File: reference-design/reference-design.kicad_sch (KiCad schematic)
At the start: 21 parts

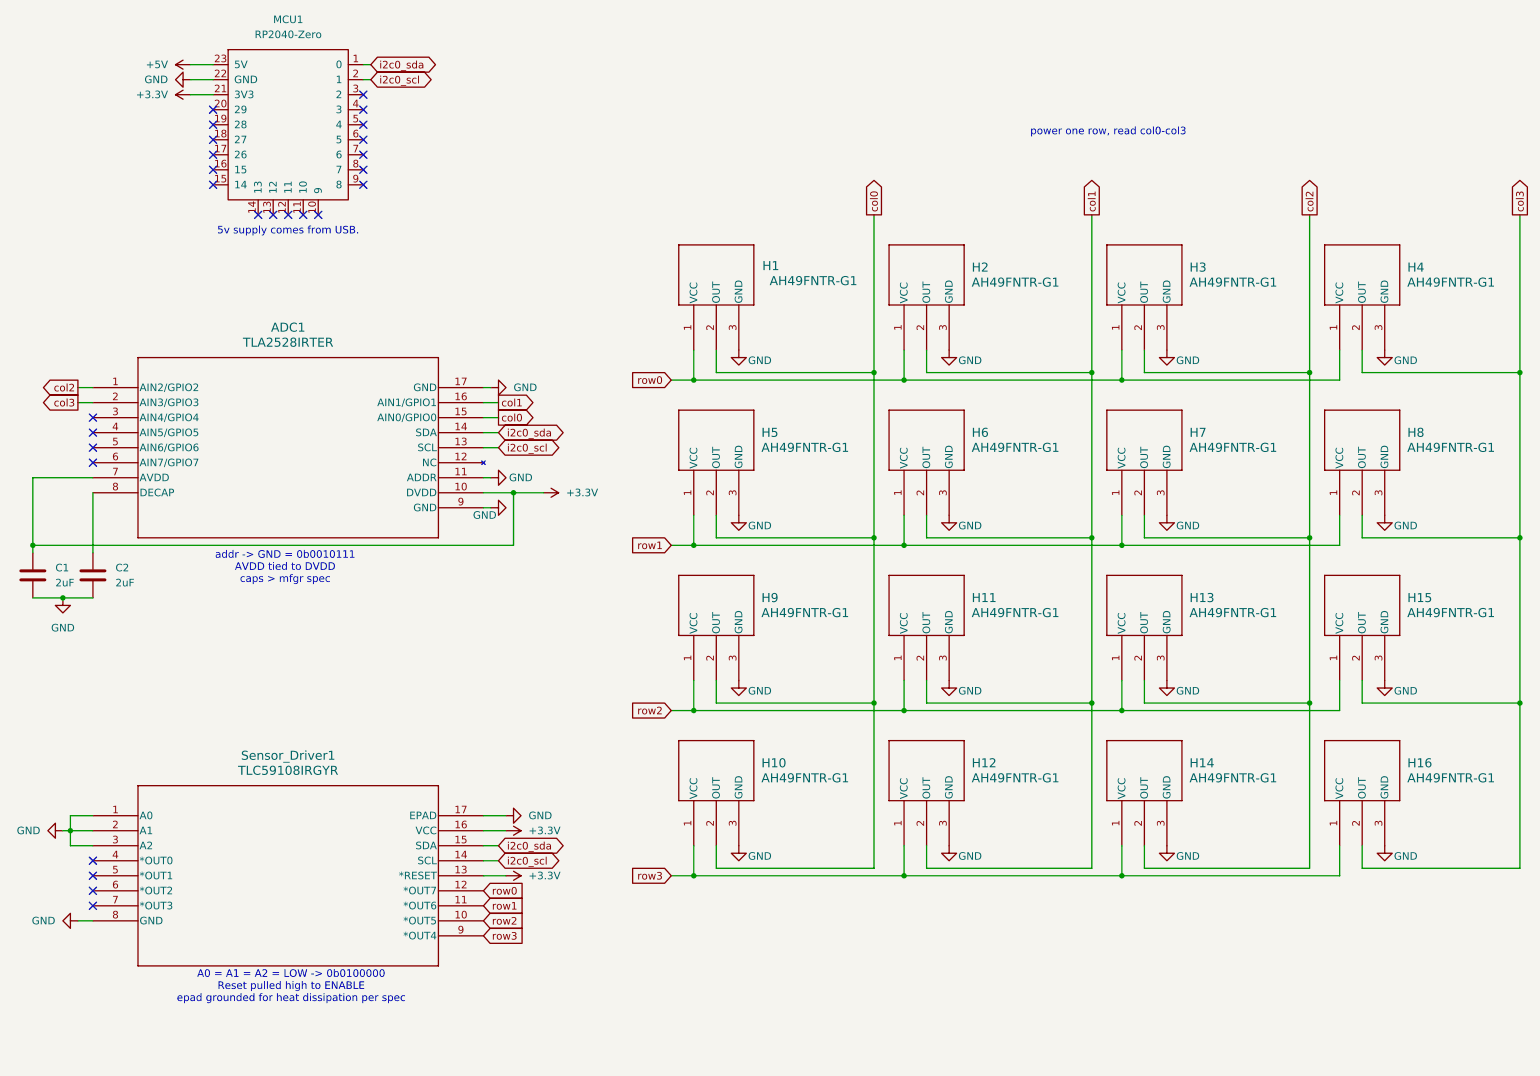
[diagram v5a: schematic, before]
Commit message: fix thermal vias
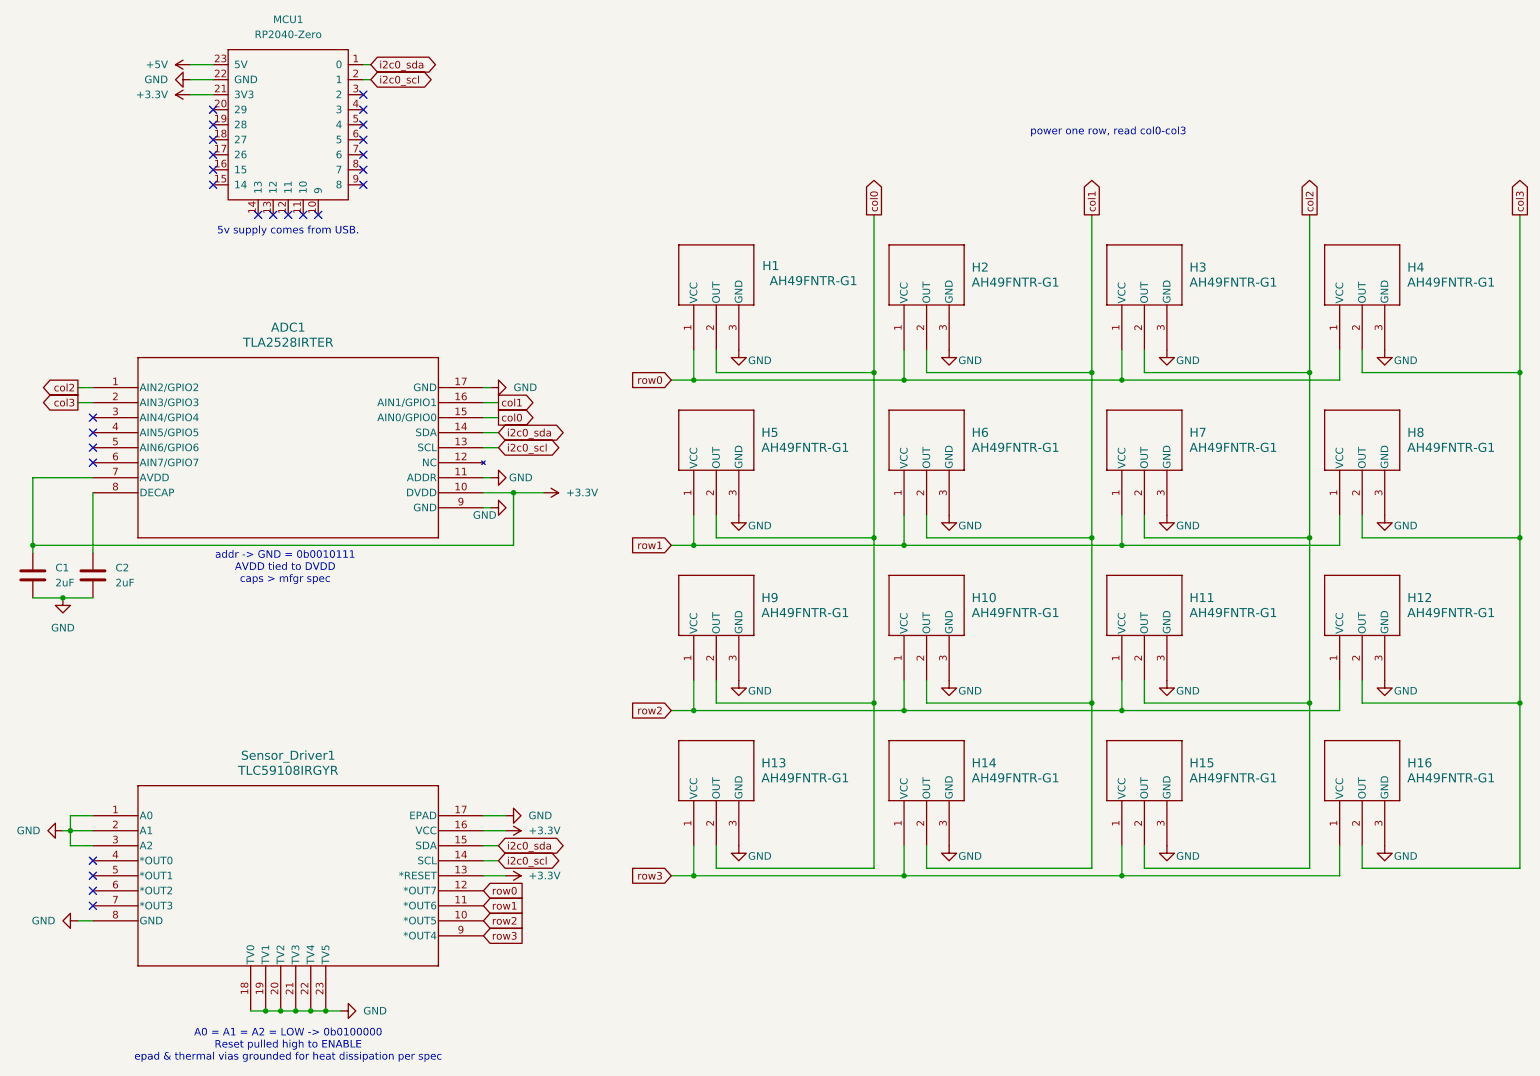
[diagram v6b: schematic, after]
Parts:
- renumbered H11 to H10, H13 to H11, H15 to H12, H10 to H13, H12 to H14, H14 to H15
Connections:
- net GND: now also Sensor_Driver1.18 (TV0), Sensor_Driver1.19 (TV1), Sensor_Driver1.20 (TV2), Sensor_Driver1.21 (TV3), Sensor_Driver1.22 (TV4), Sensor_Driver1.23 (TV5)
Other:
- note added: "A0 = A1 = A2 = LOW -> 0b0100000 Reset pulled high to ENABLE epad & thermal vias grounded for heat dissipation per spec"
- note removed: "A0 = A1 = A2 = LOW -> 0b0100000 Reset pulled high to ENABLE epad grounded for heat dissipation per spec"
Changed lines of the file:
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@@
 		)
 	)
-	(text "A0 = A1 = A2 = LOW -> 0b0100000\nReset pulled high to ENABLE\nepad grounded for heat dissipation per spec"
+	(text "A0 = A1 = A2 = LOW -> 0b0100000\nReset pulled high to ENABLE\nepad & thermal vias grounded for heat dissipation per spec"
 		(exclude_from_sim no)
-		(at 60.198 181.356 0)
+		(at 59.69 191.262 0)
 		(effects
 			(font
@@
 	)
 	(junction
+		(at 58.42 185.42)
+		(diameter 0)
+		(color 0 0 0 0)
+	)
+	(junction
 		(at 200.66 134.62)
 		(diameter 0)
@@
 	)
 	(junction
+		(at 55.88 185.42)
+		(diameter 0)
+		(color 0 0 0 0)
+	)
+	(junction
 		(at 97.79 97.79)
 		(diameter 0)
@@
 	)
 	(junction
+		(at 63.5 185.42)
+		(diameter 0)
+		(color 0 0 0 0)
+	)
+	(junction
+		(at 60.96 185.42)
+		(diameter 0)
+		(color 0 0 0 0)
+	)
+	(junction
+		(at 66.04 185.42)
+		(diameter 0)
+		(color 0 0 0 0)
+	)
+	(junction
 		(at 163.83 134.62)
 		(diameter 0)
@@
 	(wire
 		(pts
+			(xy 55.88 185.42) (xy 58.42 185.42)
+		)
+		(stroke
+			(width 0)
+			(type default)
+		)
+	)
+	(wire
+		(pts
 			(xy 237.49 101.6) (xy 237.49 106.68)
 		)
@@
 	(wire
 		(pts
+			(xy 66.04 185.42) (xy 68.58 185.42)
+		)
+		(stroke
+			(width 0)
+			(type default)
+		)
+	)
+	(wire
+		(pts
 			(xy 128.27 129.54) (xy 128.27 134.62)
 		)
@@
 	(wire
 		(pts
+			(xy 60.96 185.42) (xy 63.5 185.42)
+		)
+		(stroke
+			(width 0)
+			(type default)
+		)
+	)
+	(wire
+		(pts
 			(xy 16.51 106.68) (xy 16.51 107.95)
 		)
@@
 	(wire
 		(pts
+			(xy 58.42 185.42) (xy 60.96 185.42)
+		)
+		(stroke
+			(width 0)
+			(type default)
+		)
+	)
+	(wire
+		(pts
+			(xy 63.5 185.42) (xy 66.04 185.42)
+		)
+		(stroke
+			(width 0)
+			(type default)
+		)
+	)
+	(wire
+		(pts
 			(xy 267.97 77.47) (xy 241.3 77.47)
 		)
@@
 	(wire
 		(pts
+			(xy 53.34 185.42) (xy 55.88 185.42)
+		)
+		(stroke
+			(width 0)
+			(type default)
+		)
+	)
+	(wire
+		(pts
 			(xy 237.49 162.56) (xy 237.49 157.48)
 		)
@@
 	)
 	(symbol
+		(lib_id "power:GND")
+		(at 68.58 185.42 90)
+		(unit 1)
+		(exclude_from_sim no)
+		(in_bom yes)
+		(on_board yes)
+		(dnp no)
+		(fields_autoplaced yes)
+		(property "Reference" "#PWR031"
+			(at 74.93 185.42 0)
+			(effects
+				(font
+					(size 1.27 1.27)
+				)
+				(hide yes)
+			)
+		)
+		(property "Value" "GND"
+			(at 72.39 185.4199 90)
+			(effects
+				(font
+					(size 1.27 1.27)
+				)
+				(justify right)
+			)
+		)
+		(property "Footprint" ""
+			(at 68.58 185.42 0)
+			(effects
+				(font
+					(size 1.27 1.27)
+				)
+				(hide yes)
+			)
+		)
+		(property "Datasheet" ""
+			(at 68.58 185.42 0)
+			(effects
+				(font
+					(size 1.27 1.27)
+				)
+				(hide yes)
+			)
+		)
+		(property "Description" "Power symbol creates a global label with name \"GND\" , ground"
+			(at 68.58 185.42 0)
+			(effects
+				(font
+					(size 1.27 1.27)
+				)
+				(hide yes)
+			)
+		)
+		(pin "1"
+		)
+		(instances
+			(project "reference-design"
+				(path "/1bb90a40-7122-4522-9655-ffb2519dec46"
+					(reference "#PWR031")
+					(unit 1)
+				)
+			)
+		)
+	)
+	(symbol
 		(lib_id "Device:C")
 		(at 16.51 111.76 0)
@@
 		(dnp no)
 		(fields_autoplaced yes)
-		(property "Reference" "H14"
+		(property "Reference" "H15"
 			(at 212.09 143.5099 90)
 			(effects
@@
 			(project "reference-design"
 				(path "/1bb90a40-7122-4522-9655-ffb2519dec46"
-					(reference "H14")
+					(reference "H15")
 					(unit 1)
 				)
@@
 		(dnp no)
 		(fields_autoplaced yes)
-		(property "Reference" "H11"
+		(property "Reference" "H10"
 			(at 175.26 115.5699 90)
 			(effects
@@
 			(project "reference-design"
 				(path "/1bb90a40-7122-4522-9655-ffb2519dec46"
-					(reference "H11")
+					(reference "H10")
 					(unit 1)
 				)
@@
 		(dnp no)
 		(fields_autoplaced yes)
-		(property "Reference" "H10"
+		(property "Reference" "H13"
 			(at 139.7 143.5099 90)
 			(effects
@@
 			(project "reference-design"
 				(path "/1bb90a40-7122-4522-9655-ffb2519dec46"
-					(reference "H10")
+					(reference "H13")
 					(unit 1)
 				)
@@
 		(dnp no)
 		(fields_autoplaced yes)
-		(property "Reference" "H13"
+		(property "Reference" "H11"
 			(at 212.09 115.5699 90)
 			(effects
@@
 			(project "reference-design"
 				(path "/1bb90a40-7122-4522-9655-ffb2519dec46"
-					(reference "H13")
+					(reference "H11")
 					(unit 1)
 				)
@@
 		(pin "9"
 		)
+		(pin "23"
+		)
+		(pin "20"
+		)
+		(pin "21"
+		)
+		(pin "18"
+		)
+		(pin "22"
+		)
+		(pin "19"
+		)
 		(instances
 			(project ""
@@
 		(dnp no)
 		(fields_autoplaced yes)
-		(property "Reference" "H15"
+		(property "Reference" "H12"
 			(at 248.92 115.5699 90)
 			(effects
@@
 			(project "reference-design"
 				(path "/1bb90a40-7122-4522-9655-ffb2519dec46"
-					(reference "H15")
+					(reference "H12")
 					(unit 1)
 				)
@@
 		(dnp no)
 		(fields_autoplaced yes)
-		(property "Reference" "H12"
+		(property "Reference" "H14"
 			(at 175.26 143.5099 90)
 			(effects
@@
 			(project "reference-design"
 				(path "/1bb90a40-7122-4522-9655-ffb2519dec46"
-					(reference "H12")
+					(reference "H14")
 					(unit 1)
 				)
